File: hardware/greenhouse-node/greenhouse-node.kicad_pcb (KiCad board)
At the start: 2 copper layers, 90.2 x 69.8 mm, 54 parts, among them J1 Conn_01x12_Male, J2 Conn_01x02_Male, J3 Conn_01x02_Male, J4 Conn_01x02_Male, J5 Conn_01x04_Male, J6 RX_PinHeader_1x04_P2.54mm, J7 TX_PinHeader_1x04_P2.54mm, J8 Conn_01x02_Male, Q1 BC549C, Q2 BC549C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

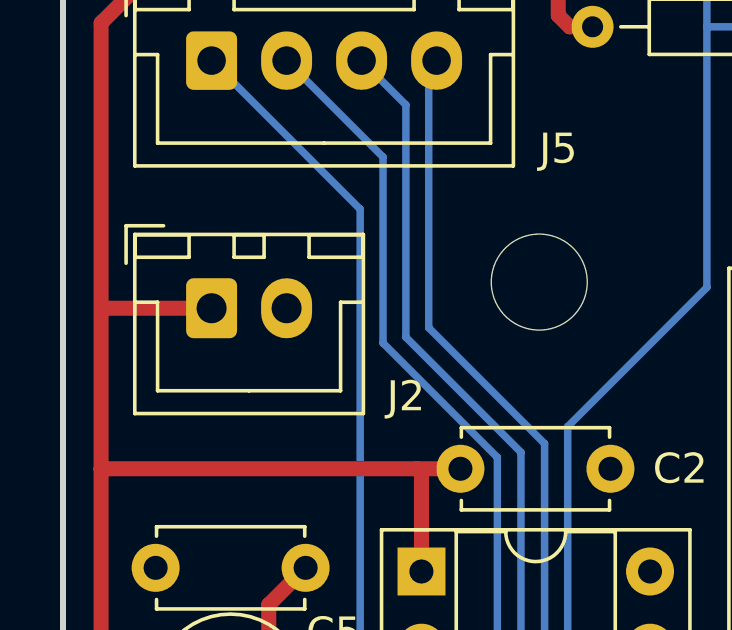
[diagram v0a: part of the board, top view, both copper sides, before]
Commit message: Swapped GND/PWR for IC programming connector
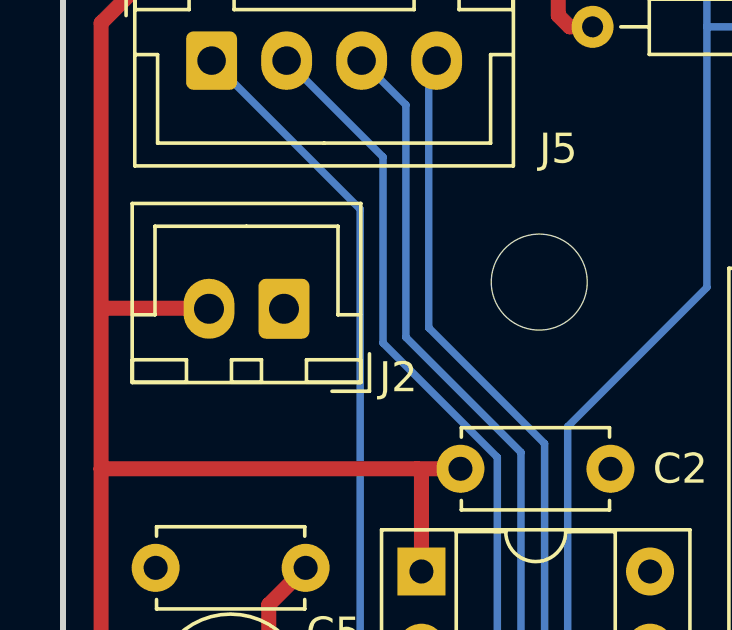
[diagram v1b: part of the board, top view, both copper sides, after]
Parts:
- moved J2 2.41 mm to (67.3, 46.5), turned to 180 degrees
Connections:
- J2 pad 1: +5V -> GND
- J2 pad 2: GND -> +5V
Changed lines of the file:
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@@
   )
   (footprint "Connector_JST:JST_XH_B2B-XH-A_1x02_P2.50mm_Vertical" (layer "F.Cu")
-    (at 64.897 46.465)
+    (at 67.31 46.482 180)
     (descr "JST XH series connector, B2B-XH-A (http://www.jst-mfg.com/product/pdf/eng/eXH.pdf), generated with kicad-footprint-generator")
     (tags "connector JST XH vertical")
@@
     (property "Sheetname" "")
     (attr through_hole)
-    (fp_text reference "J2" (at 6.477 2.938) (layer "F.SilkS")
-      (effects (font (size 1 1) (thickness 0.15)))
-    )
-    (fp_text value "Conn_01x02_Male" (at 1.25 4.6) (layer "F.Fab")
+    (fp_text reference "J2" (at -3.81 -2.286) (layer "F.SilkS")
+      (effects (font (size 1 1) (thickness 0.15)))
+    )
+    (fp_text value "Conn_01x02_Male" (at 0.762 -3.556) (layer "F.Fab")
       (effects (font (size 1 1) (thickness 0.15)))
     )
@@
     (fp_line (start 0 -1.35) (end 0.625 -2.35) (layer "F.Fab") (width 0.1))
     (fp_line (start 4.95 -2.35) (end -2.45 -2.35) (layer "F.Fab") (width 0.1))
-    (pad "1" thru_hole roundrect (at 0 0) (size 1.7 2) (drill 1) (layers *.Cu *.Mask) (roundrect_rratio 0.147059)
-      (net 1 "+5V") (pinfunction "Pin_1") (pintype "passive"))
-    (pad "2" thru_hole oval (at 2.5 0) (size 1.7 2) (drill 1) (layers *.Cu *.Mask)
-      (net 2 "GND") (pinfunction "Pin_2") (pintype "passive"))
+    (pad "1" thru_hole roundrect (at 0 0 180) (size 1.7 2) (drill 1) (layers *.Cu *.Mask) (roundrect_rratio 0.147059)
+      (net 2 "GND") (pinfunction "Pin_1") (pintype "passive"))
+    (pad "2" thru_hole oval (at 2.5 0 180) (size 1.7 2) (drill 1) (layers *.Cu *.Mask)
+      (net 1 "+5V") (pinfunction "Pin_2") (pintype "passive"))
     (model "${KICAD6_3DMODEL_DIR}/Connector_JST.3dshapes/JST_XH_B2B-XH-A_1x02_P2.50mm_Vertical.wrl"
       (offset (xyz 0 0 0))
@@
       (effects (font (size 1 1) (thickness 0.15)))
     )
-    (fp_text value "Conn_01x04_Male" (at 3.75 4.6) (layer "F.Fab")
+    (fp_text value "Conn_01x04_Male" (at 3.429 -3.158) (layer "F.Fab")
       (effects (font (size 1 1) (thickness 0.15)))
     )
@@
     (connect_pads (clearance 0))
     (min_thickness 0.254)
-    (keepout (tracks not_allowed) (vias not_allowed) (pads not_allowed) (copperpour not_allowed) (footprints allowed))
+    (keepout (tracks not_allowed) (vias not_allowed) (pads not_allowed ) (copperpour not_allowed) (footprints allowed))
     (fill (thermal_gap 0.508) (thermal_bridge_width 0.508))
     (polygon
@@
     (connect_pads (clearance 0))
     (min_thickness 0.254)
-    (keepout (tracks not_allowed) (vias not_allowed) (pads not_allowed) (copperpour not_allowed) (footprints allowed))
+    (keepout (tracks not_allowed) (vias not_allowed) (pads not_allowed ) (copperpour not_allowed) (footprints allowed))
     (fill (thermal_gap 0.508) (thermal_bridge_width 0.508))
     (polygon

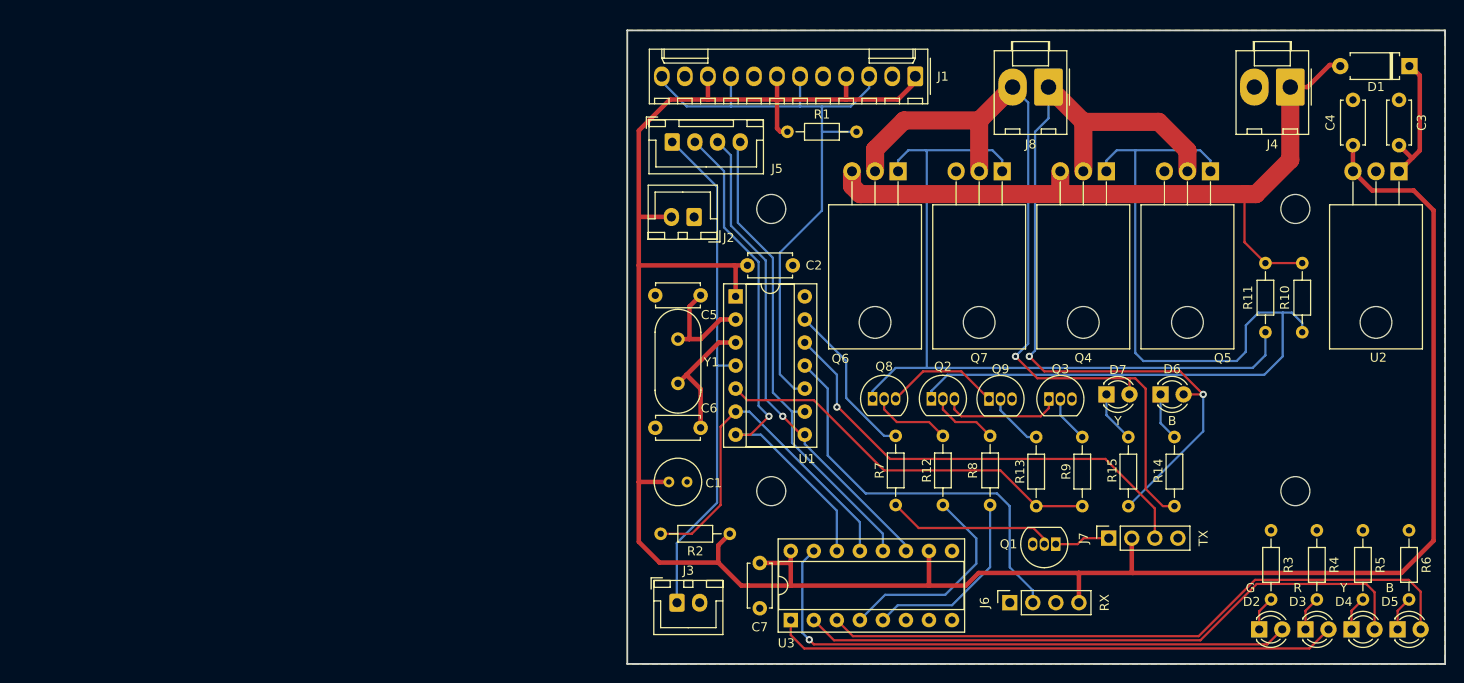
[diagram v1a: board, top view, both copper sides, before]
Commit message: Replace RX/TX modules with HC-12
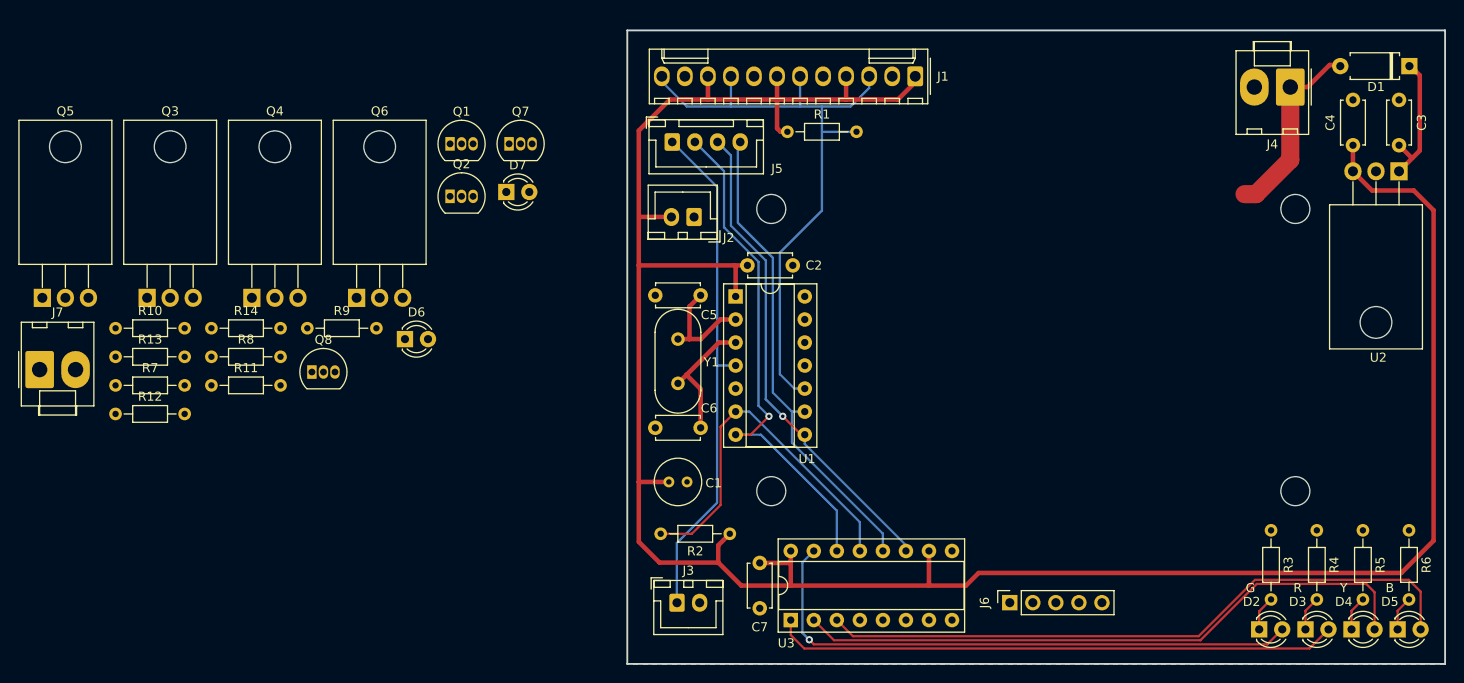
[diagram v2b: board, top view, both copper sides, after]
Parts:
- removed J8: Conn_01x02_Male, Connector_Molex:Molex_KK-396_A-41791-0002_1x02_P3.96mm_Vertical
- removed Q9: BC549C, Package_TO_SOT_THT:TO-92_Inline
- removed R15: 1k, Resistor_THT:R_Axial_DIN0204_L3.6mm_D1.6mm_P7.62mm_Horizontal
- J6: value RX_PinHeader_1x04_P2.54mm -> Conn_01x05_Female; footprint Connector_PinSocket_2.54mm:PinSocket_1x04_P2.54mm_Vertical -> Connector_PinSocket_2.54mm:PinSocket_1x05_P2.54mm_Vertical
- J7: value TX_PinHeader_1x04_P2.54mm -> Conn_01x02_Male; footprint Connector_PinSocket_2.54mm:PinSocket_1x04_P2.54mm_Vertical -> Connector_Molex:Molex_KK-396_A-41791-0002_1x02_P3.96mm_Vertical
- Q3: value BC549C -> IRF9530N; footprint Package_TO_SOT_THT:TO-92_Inline -> Package_TO_SOT_THT:TO-220-3_Horizontal_TabDown
- Q4, Q6: value IRF9530N -> IRF530N
- Q5: value IRF530N -> IRF9530N
- Q7: value IRF530N -> BC549C; footprint Package_TO_SOT_THT:TO-220-3_Horizontal_TabDown -> Package_TO_SOT_THT:TO-92_Inline
- R10: value 2k -> 5k
- R11: value 2k -> 1k
- R12, R9: value 1k -> 2k
- R14, R7: value 5k -> 1k
- moved R10 130.8 mm to (3.52, 58.7), turned to 0 degrees
- moved Q5 129.5 mm to (-4.55, 55.4), turned to 0 degrees
- moved J7 119.3 mm to (-4.85, 63.3), turned to 0 degrees
- moved R11 116.4 mm to (14.1, 65.0), turned to 0 degrees
- moved R14 108.0 mm to (14.1, 58.7), turned to 0 degrees
- moved R13 101.9 mm to (3.52, 61.9), turned to 0 degrees
- moved Q3 100.0 mm to (7.00, 55.4)
- moved Q4 95.2 mm to (18.6, 55.4), turned to 0 degrees
- moved R12 91.3 mm to (3.52, 68.2), turned to 0 degrees
- moved R7 87.0 mm to (3.52, 65.0), turned to 0 degrees
- moved R8 86.3 mm to (14.1, 61.9), turned to 0 degrees
- moved R9 86.3 mm to (24.7, 58.7), turned to 0 degrees
- moved D6 83.5 mm to (35.4, 59.9)
- moved Q1 80.1 mm to (40.4, 38.4), turned to 0 degrees
- moved D7 69.8 mm to (46.6, 43.7)
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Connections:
- D6 pad 2: /motor/Motor_1 -> /Motor_1
- D7 pad 2: /motor/Motor_2 -> /Motor_2
- J6 pad 1: GND -> +5V
- J6 pad 2: /RAD_RX -> GND
- J6 pad 3: unconnected-(J6-Pad3) -> /RAD_RX
- J6 pad 4: +5V -> /RAD_TX
- J7 pad 1: Net-(J7-Pad1) -> /Motor_1
- J7 pad 2: +5V -> /Motor_2
- Q1 pad 1: Net-(J7-Pad1) -> Net-(Q1-Pad1)
- Q1 pad 3: GND -> Net-(Q1-Pad3)
- Q2 pad 1: Net-(Q2-Pad1) -> Net-(Q1-Pad3)
- Q2 pad 3: Net-(Q2-Pad3) -> GND
- Q3 pad 1: Net-(Q2-Pad3) -> Net-(Q1-Pad1)
- Q3 pad 2: Net-(Q3-Pad2) -> /Motor_1
- Q3 pad 3: GND -> +10V
- Q4 pad 1: Net-(Q2-Pad1) -> Net-(Q1-Pad1)
- Q4 pad 2: /motor/Motor_1 -> /Motor_1
- Q4 pad 3: +10V -> GND
- Q5 pad 1: Net-(Q2-Pad1) -> Net-(Q5-Pad1)
- Q5 pad 2: /motor/Motor_1 -> /Motor_2
- Q5 pad 3: GND -> +10V
- Q6 pad 1: Net-(Q6-Pad1) -> Net-(Q5-Pad1)
- Q6 pad 2: /motor/Motor_2 -> /Motor_2
- Q6 pad 3: +10V -> GND
- Q7 pad 1: Net-(Q6-Pad1) -> Net-(Q5-Pad1)
- Q7 pad 2: /motor/Motor_2 -> Net-(Q7-Pad2)
- Q7 pad 3: GND -> Net-(Q7-Pad3)
- Q8 pad 1: Net-(Q6-Pad1) -> Net-(Q7-Pad3)
- Q8 pad 3: Net-(Q8-Pad3) -> GND
- R10 pad 1: Net-(Q2-Pad1) -> /Motor_2
- R10 pad 2: +10V -> Net-(D6-Pad1)
- R11 pad 1: Net-(Q6-Pad1) -> /Motor_1
- R11 pad 2: +10V -> Net-(D7-Pad1)
- R12 pad 1: Net-(Q8-Pad2) -> Net-(Q5-Pad1)
- R12 pad 2: Motor_B -> +10V
- R13 pad 1: Net-(Q9-Pad2) -> Net-(Q7-Pad2)
- R13 pad 2: Motor_PWM -> Motor_B
- R14 pad 1: /motor/Motor_2 -> Net-(Q8-Pad2)
- R14 pad 2: Net-(D6-Pad1) -> Motor_PWM
- R7 pad 2: /RAD_TX_EN -> Motor_A
- R8 pad 2: Motor_A -> Motor_PWM
- R9 pad 1: Net-(Q3-Pad2) -> Net-(Q1-Pad1)
- R9 pad 2: Motor_PWM -> +10V
- U1 pad 13: /RAD_TX_EN -> unconnected-(U1-Pad13)
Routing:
- net Net-(Q2-Pad1): track 107.3 -> 0.00 mm
- net /motor/Motor_1: track 95.3 -> 0.00 mm, vias 2 -> 0
- net /motor/Motor_2: track 89.6 -> 0.00 mm, vias 1 -> 0
- net Net-(Q6-Pad1): track 87.1 -> 0.00 mm
- net +10V: track 82.4 -> 21.9 mm
- net /RAD_TX: track 51.5 -> 0.00 mm, vias 1 -> 0
- net /RAD_RX: track 45.0 -> 0.00 mm
- net Motor_PWM: track 43.6 -> 0.00 mm
- net Motor_B: track 23.4 -> 0.00 mm
- net Motor_A: track 21.1 -> 0.00 mm
- net Net-(Q1-Pad2): track 18.5 -> 0.00 mm
- net /RAD_TX_EN: track 17.7 -> 0.00 mm
- net Net-(Q2-Pad3): track 13.3 -> 0.00 mm
- net Net-(Q8-Pad3): track 12.8 -> 0.00 mm
- net Net-(Q8-Pad2): track 8.85 -> 0.00 mm
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
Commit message: Moved voltage drop to nodes
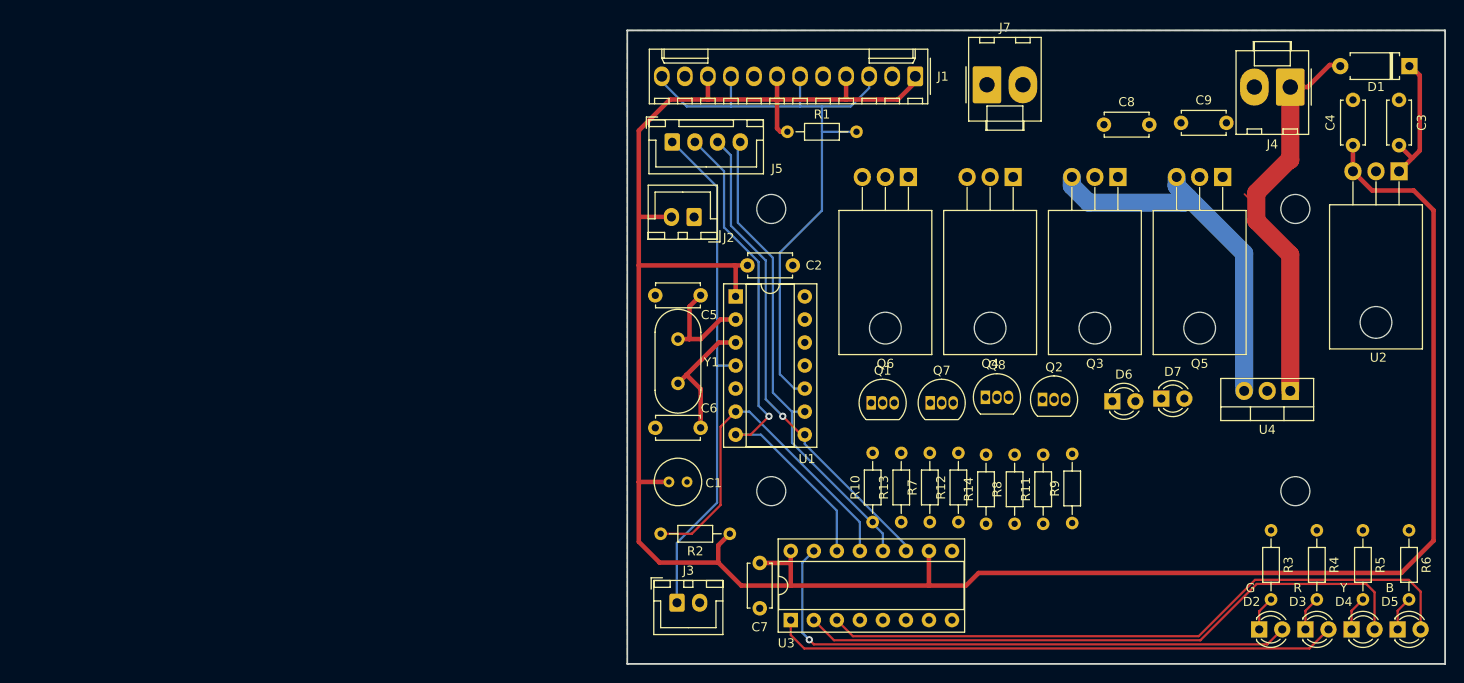
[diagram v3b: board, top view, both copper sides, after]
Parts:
- removed J6: Conn_01x05_Female, Connector_PinSocket_2.54mm:PinSocket_1x05_P2.54mm_Vertical
- added C8: 330nF, Capacitor_THT:C_Disc_D4.7mm_W2.5mm_P5.00mm, F.Cu at (112.5, 36.3)
- added C9: 100nF, Capacitor_THT:C_Disc_D4.7mm_W2.5mm_P5.00mm, F.Cu at (121.0, 36.1)
- added U4: L7810, Package_TO_SOT_THT:TO-220-3_Vertical, F.Cu at (133.0, 65.7)
- moved Q5 130.8 mm to (125.6, 42.1), turned to 180 degrees
- moved J7 109.1 mm to (99.6, 31.9)
- moved Q3 107.9 mm to (114.0, 42.1), turned to 180 degrees
- moved R12 93.7 mm to (96.5, 80.1), turned to 90 degrees
- moved R11 93.0 mm to (105.8, 80.3), turned to 90 degrees
- moved R7 91.0 mm to (93.3, 80.1), turned to 90 degrees
- moved R8 90.5 mm to (102.7, 80.3), turned to 90 degrees
- moved R13 88.5 mm to (90.2, 80.1), turned to 90 degrees
- moved R14 88.1 mm to (99.5, 80.3), turned to 90 degrees
- moved R9 87.0 mm to (109.0, 80.2), turned to 90 degrees
- moved R10 86.2 mm to (87.0, 80.1), turned to 90 degrees
- moved Q4 85.0 mm to (102.5, 42.1), turned to 180 degrees
- moved D6 78.3 mm to (113.4, 66.8)
- moved D7 75.7 mm to (118.8, 66.5)
- moved Q8 74.3 mm to (99.4, 66.4)
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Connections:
- J4 pad 1: +10V -> +12V
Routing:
- net /SR_RCLK: track 52.9 -> 0.00 mm
- net /SR_CLK: track 52.9 -> 105.8 mm
- net +12V: track 0.00 -> 43.9 mm
- net +10V: track 21.9 -> 41.5 mm

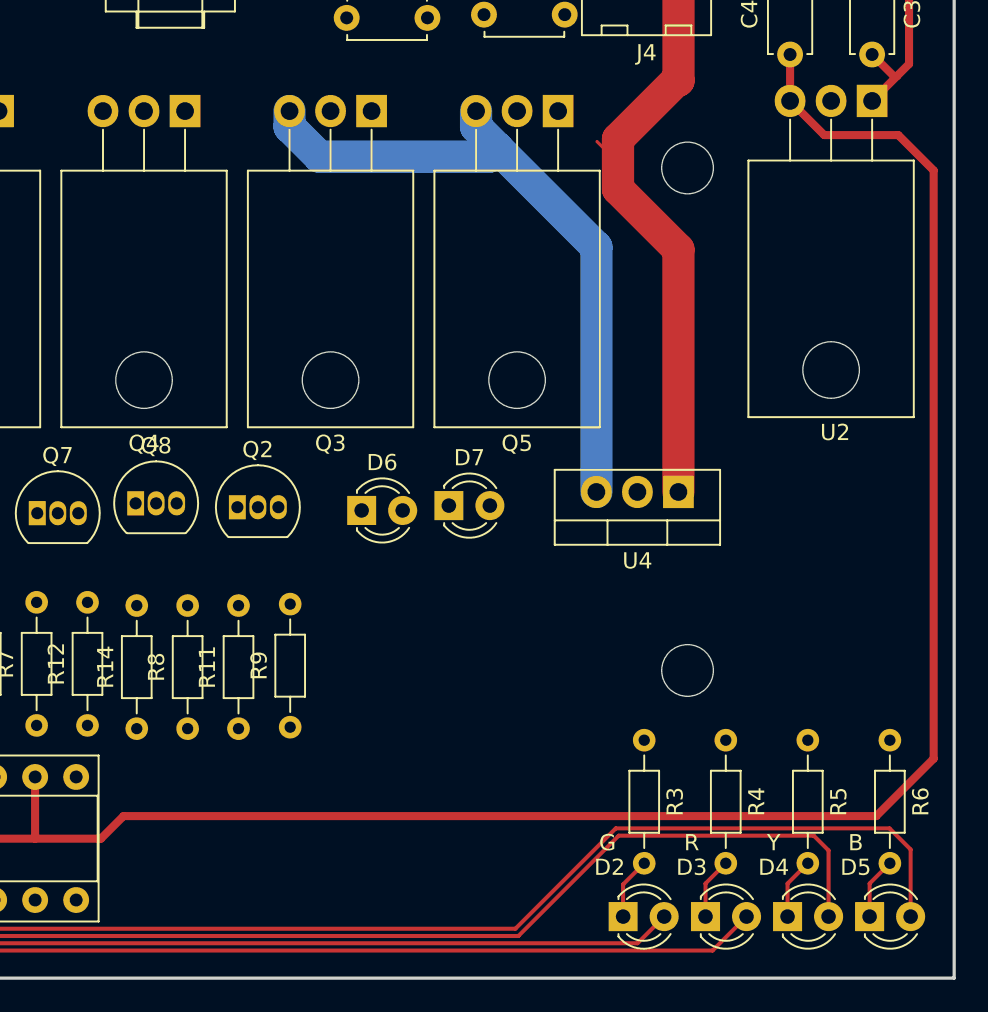
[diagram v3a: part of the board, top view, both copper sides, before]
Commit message: Implement HC-12 on node
Also removed switch logic and old shift register
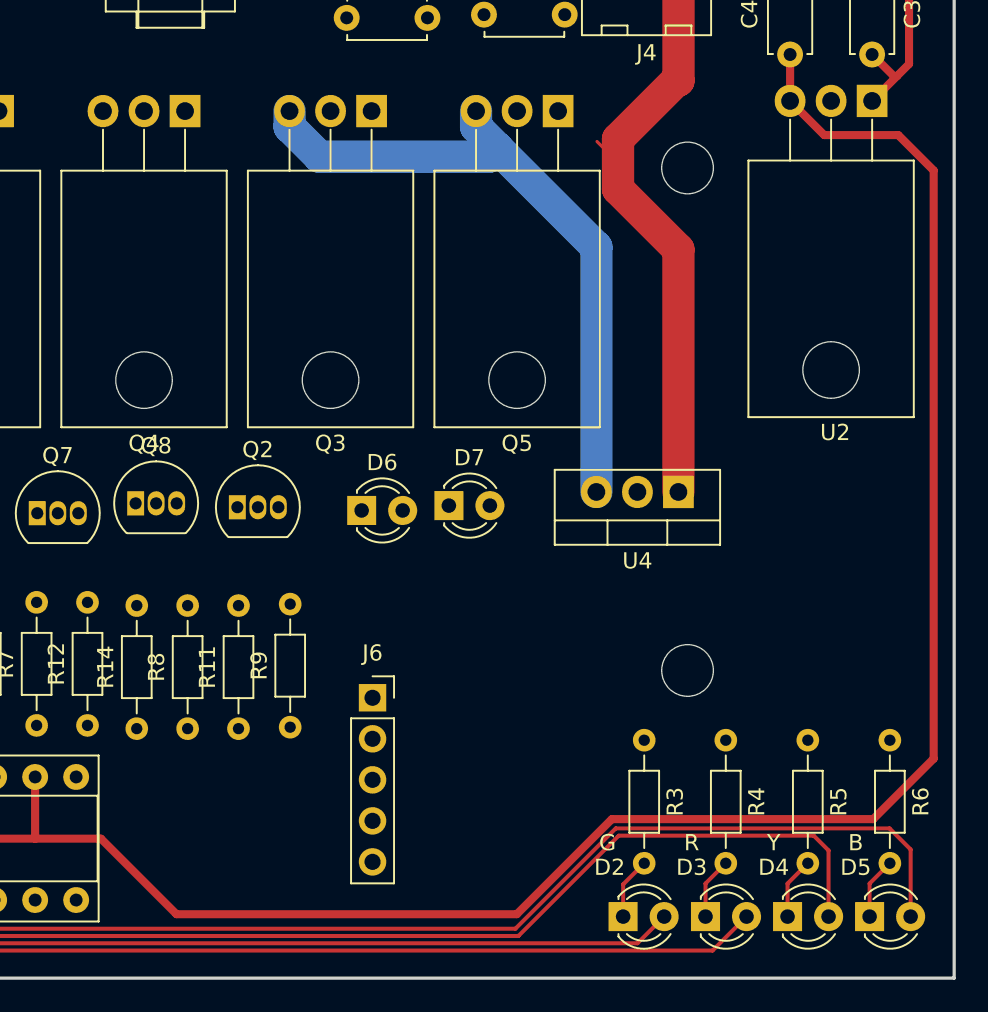
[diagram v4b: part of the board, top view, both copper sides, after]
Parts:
- added J6: Conn_01x05_Female, Connector_PinSocket_2.54mm:PinSocket_1x05_P2.54mm_Vertical, F.Cu at (114.1, 78.4)
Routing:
- net /SR_RCLK: track 0.00 -> 105.8 mm, vias 0 -> 1
- net /SR_CLK: track 105.8 -> 0.00 mm, vias 1 -> 0
- net +5V: track 269.0 -> 272.8 mm
